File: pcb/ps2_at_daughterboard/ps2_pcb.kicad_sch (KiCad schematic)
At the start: 18 parts, among them J1 Conn_02x03_Odd_Even, J2 USB_C_Receptacle_USB2.0, Q1 BSS138, Q2 BSS138, U2 MIC2009A-1YM6, U3 USBLC6-2SC6

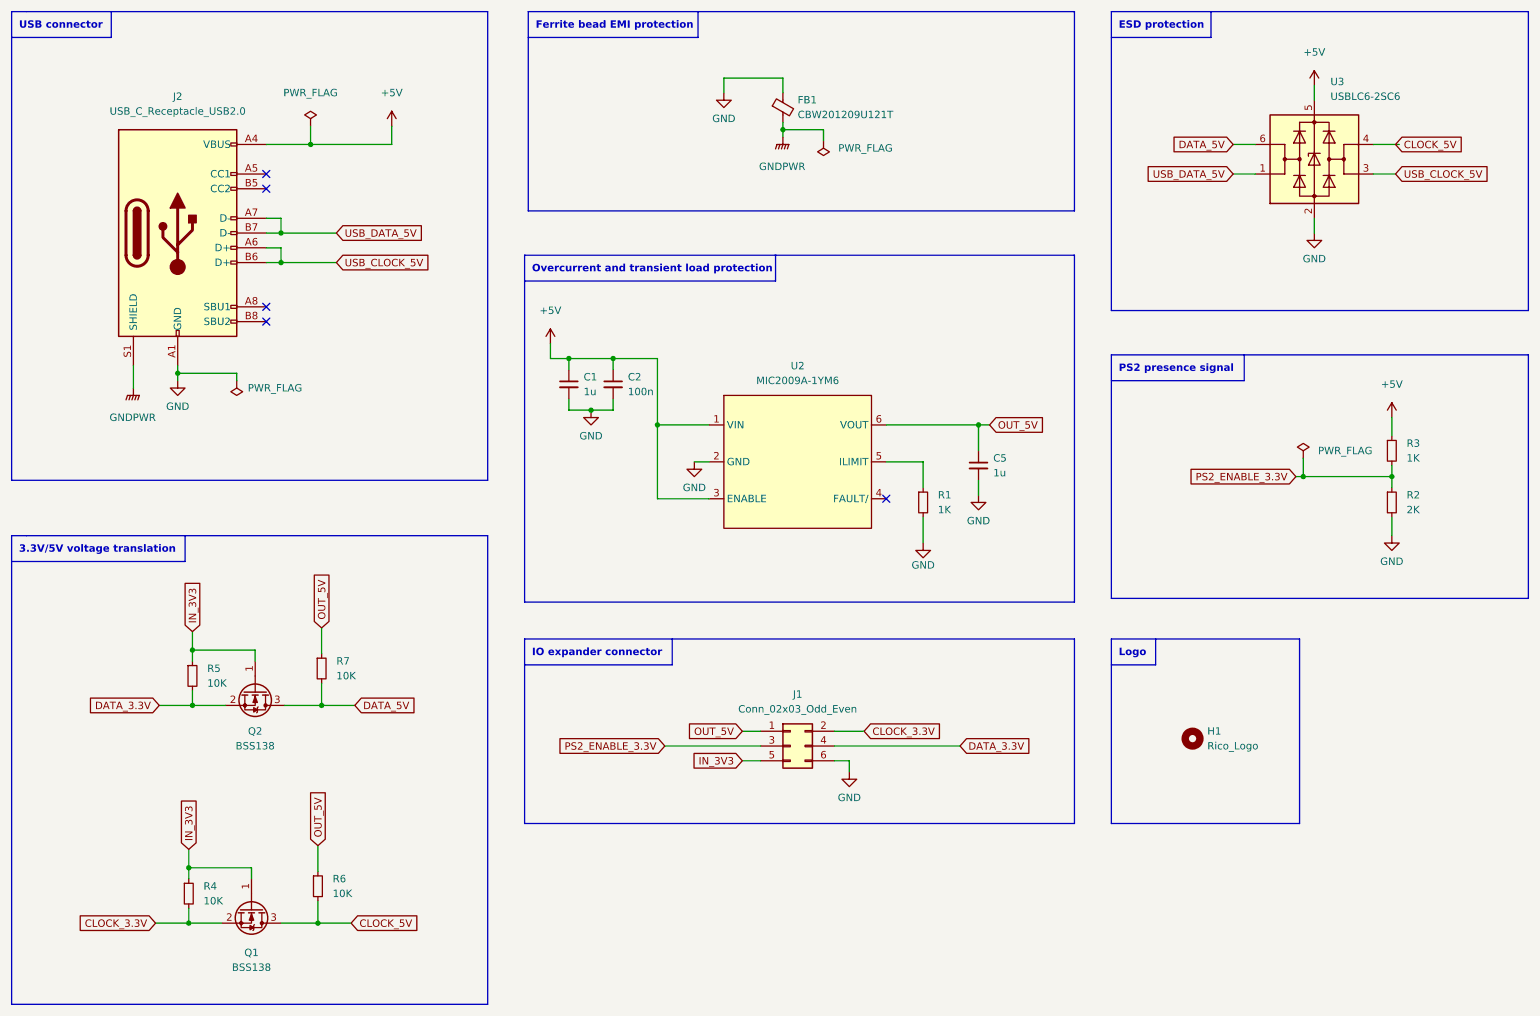
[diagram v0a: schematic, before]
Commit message: [feature] PS2 daughterboard project conversion to Kicad 10.x
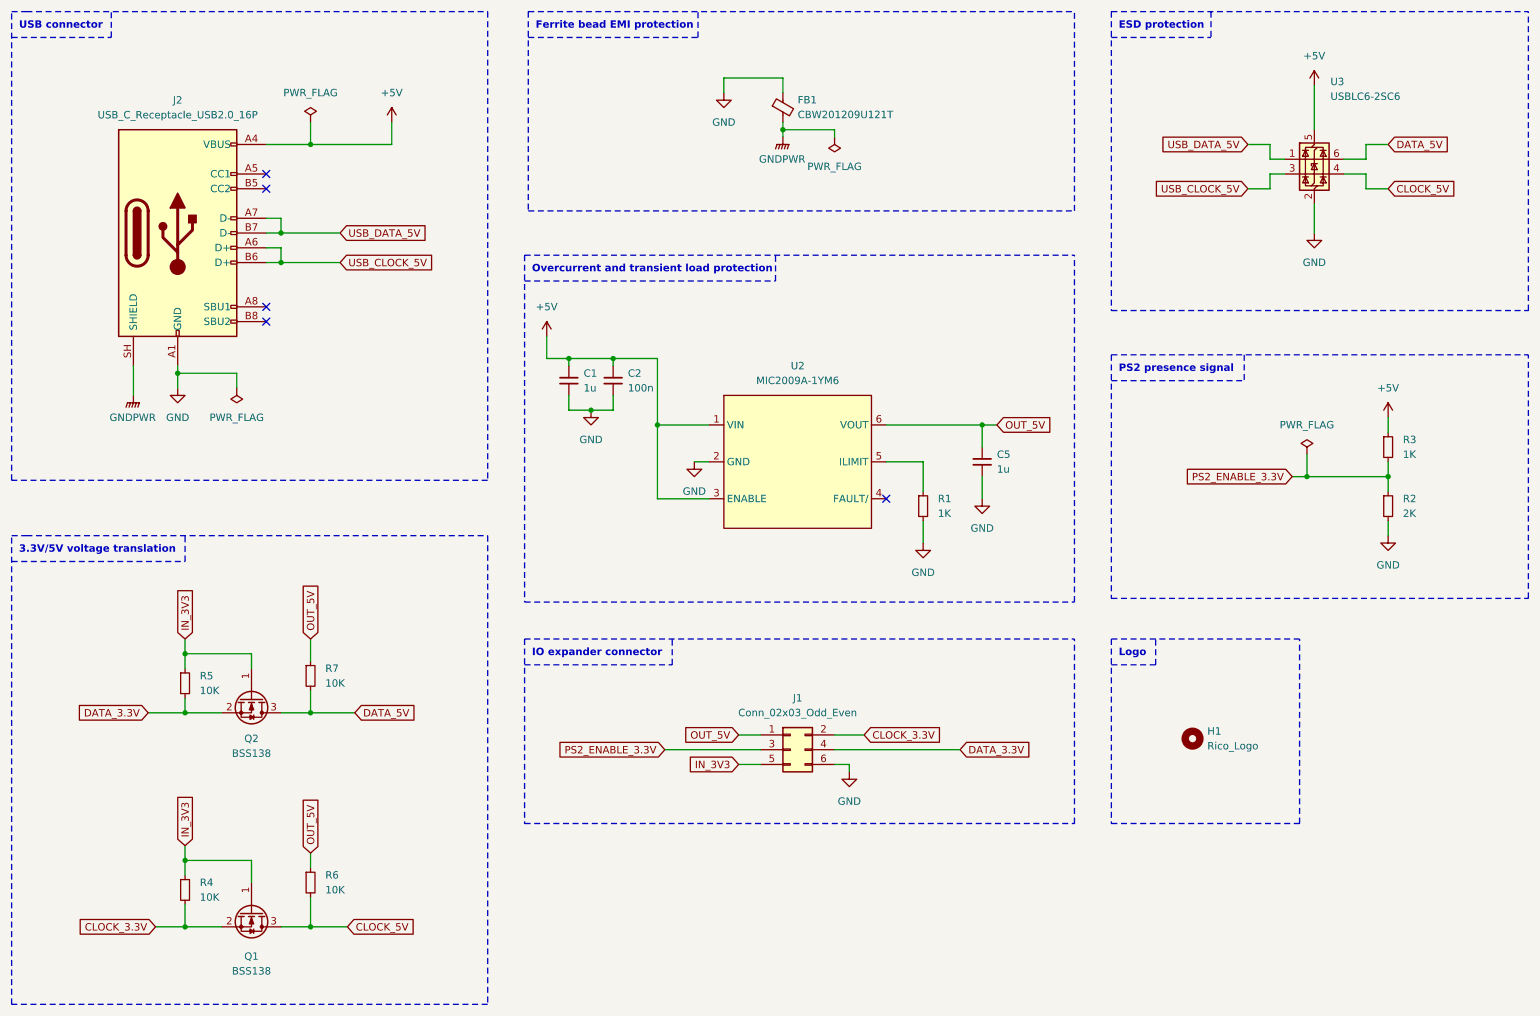
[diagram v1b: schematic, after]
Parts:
- removed J2: USB_C_Receptacle_USB2.0, Model-F:USB_C_Receptacle_HRO_TYPE-C-31-M-12, symbol Connector:USB_C_Receptacle_USB2.0
- added J2: USB_C_Receptacle_USB2.0_16P, Model-F:USB_C_Receptacle_HRO_TYPE-C-31-M-12, symbol Connector:USB_C_Receptacle_USB2.0_16P
- Q1, Q2: footprint Model-F:SOT-23 -> Package_TO_SOT_SMD:SOT-23
- U3: footprint Model-F:SOT-23-6 -> Package_TO_SOT_SMD:SOT-23-6
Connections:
- net +5V: now also J2.A4 (VBUS), J2.A9 (VBUS), J2.B4 (VBUS), J2.B9 (VBUS)
- net GND: now also J2.A1 (GND), J2.A12 (GND), J2.B1 (GND), J2.B12 (GND)
- net GNDPWR: now also J2.SH (SHIELD)
- net USB_CLOCK_5V: now also J2.A6 (D+), J2.B6 (D+)
- net USB_DATA_5V: now also J2.A7 (D-), J2.B7 (D-)
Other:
- moved on the sheet: C1, C2, C5, J1, Q1, Q2, R1, R2, R3, R4, R5, R6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

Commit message: [feature] PS2 daughterboard design Rev 2 ready for fabrication.
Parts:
- added D1: D_Schottky_Small, Model-F:D_SOD-123, symbol Device:D_Schottky_Small
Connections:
- net OUT_5V: now also D1.2 (A); no longer J1.1 (Pin_1)
- new net CONN_5V: D1.1 (K), J1.1 (Pin_1)
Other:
- moved on the sheet: C5, H1

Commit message: [bugfix] Wrong 0402 casings instead of 0603.
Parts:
- C1, C5: LCSC C52923 -> C15849
- C2: LCSC C1525 -> C1590
- R1, R3: LCSC C11702 -> C21190
- R2: LCSC C100291 -> C22975
- R4, R5, R6, R7: LCSC C25744 -> C25804
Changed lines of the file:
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@@
 			)
 		)
-		(property "LCSC" "C11702"
+		(property "LCSC" "C21190"
 			(at 255.27 92.71 0)
 			(hide yes)
@@
 			)
 		)
-		(property "LCSC" "C25744"
+		(property "LCSC" "C25804"
 			(at 69.85 132.08 0)
 			(hide yes)
@@
 			)
 		)
-		(property "LCSC" "C100291"
+		(property "LCSC" "C22975"
 			(at 255.27 102.87 0)
 			(hide yes)
@@
 			)
 		)
-		(property "LCSC" "C25744"
+		(property "LCSC" "C25804"
 			(at 69.85 167.64 0)
 			(hide yes)
@@
 			)
 		)
-		(property "LCSC" "C52923"
+		(property "LCSC" "C15849"
 			(at 114.3 81.28 0)
 			(hide yes)
@@
 			)
 		)
-		(property "LCSC" "C1525"
+		(property "LCSC" "C1590"
 			(at 121.92 81.28 0)
 			(hide yes)
@@
 			)
 		)
-		(property "LCSC" "C11702"
+		(property "LCSC" "C21190"
 			(at 175.26 102.87 0)
 			(hide yes)
@@
 			)
 		)
-		(property "LCSC" "C25744"
+		(property "LCSC" "C25804"
 			(at 48.26 133.35 0)
 			(hide yes)
@@
 			)
 		)
-		(property "LCSC" "C25744"
+		(property "LCSC" "C25804"
 			(at 48.26 168.91 0)
 			(hide yes)
@@
 			)
 		)
-		(property "LCSC" "C52923"
+		(property "LCSC" "C15849"
 			(at 184.15 102.87 0)
 			(hide yes)
